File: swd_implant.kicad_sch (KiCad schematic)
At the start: 21 parts, among them J1 U262-161N-4BVC11, J2 G&W pressure contact, J3 50 mil Pin Header, J4 SOICbite, J5 100 mil Pin Header, J6 100 mil Pin header, U1 ATSAMD21E18A, U2 AP2127K-3.3

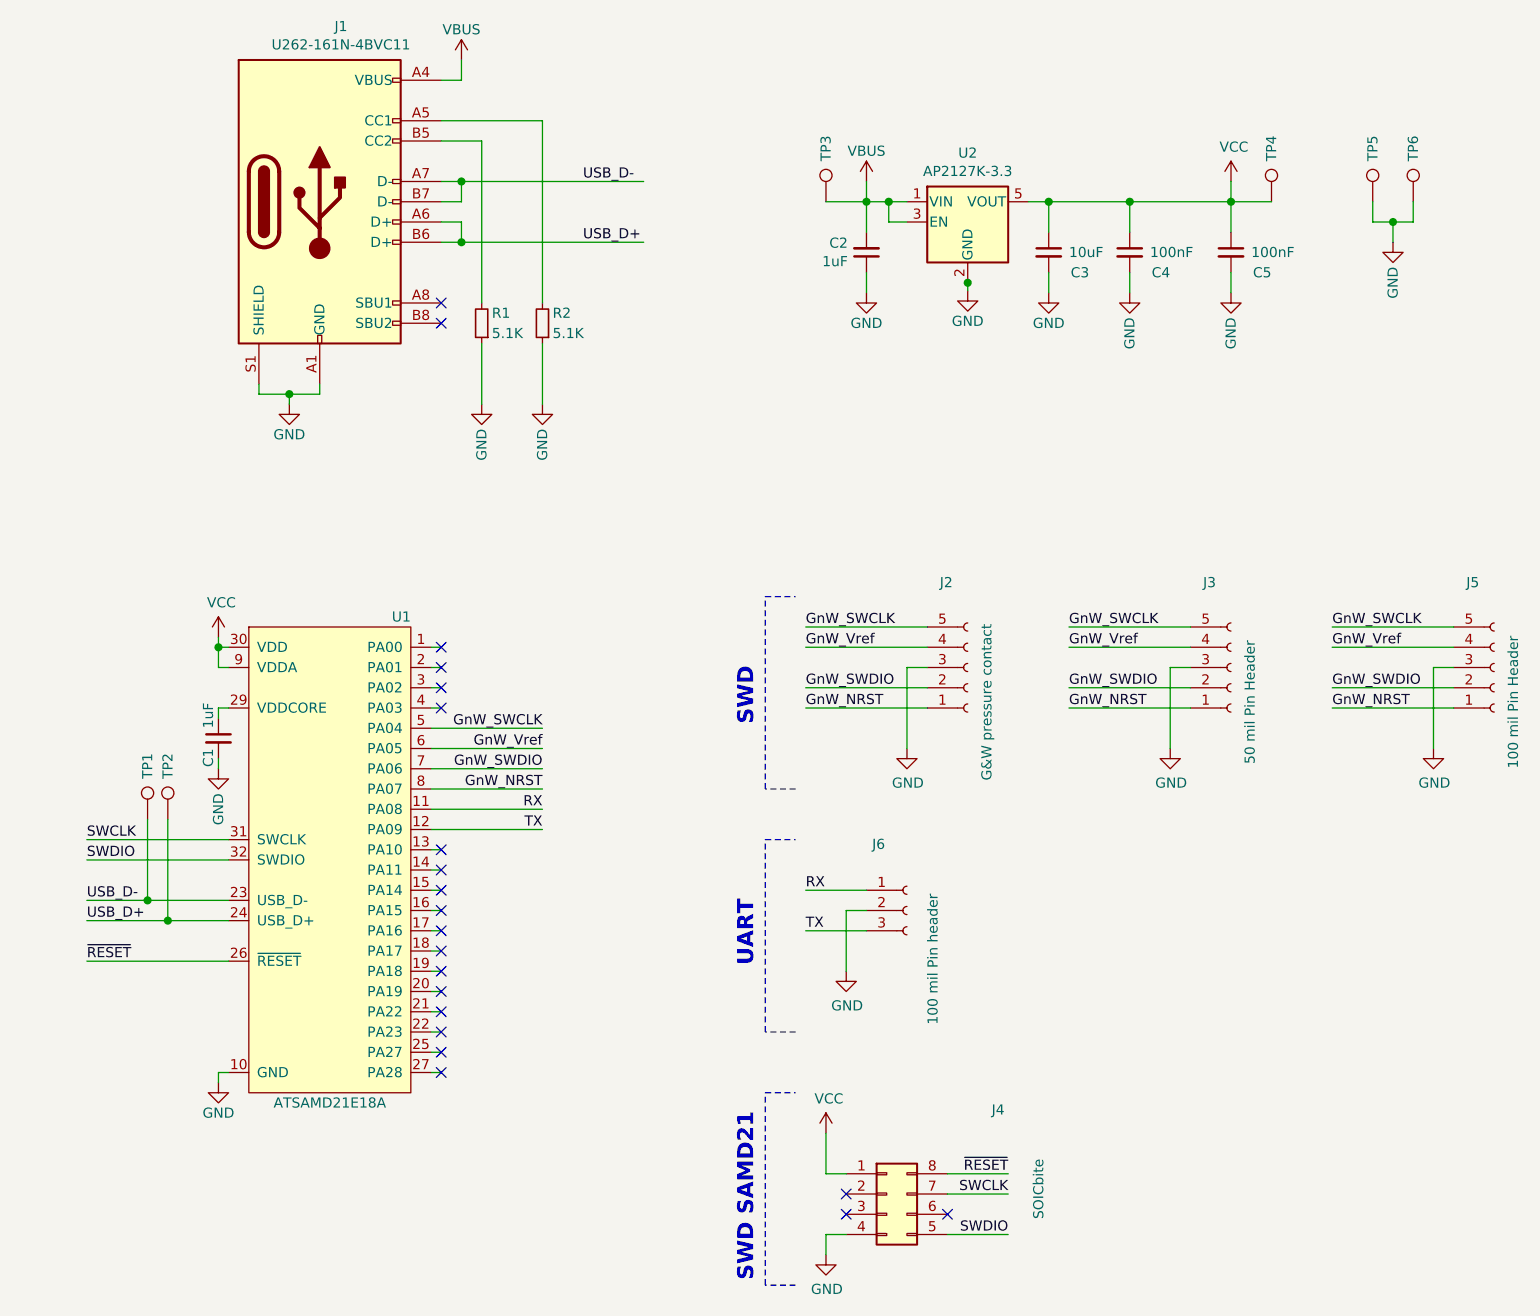
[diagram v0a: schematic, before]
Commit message: Added 10k reset pullup
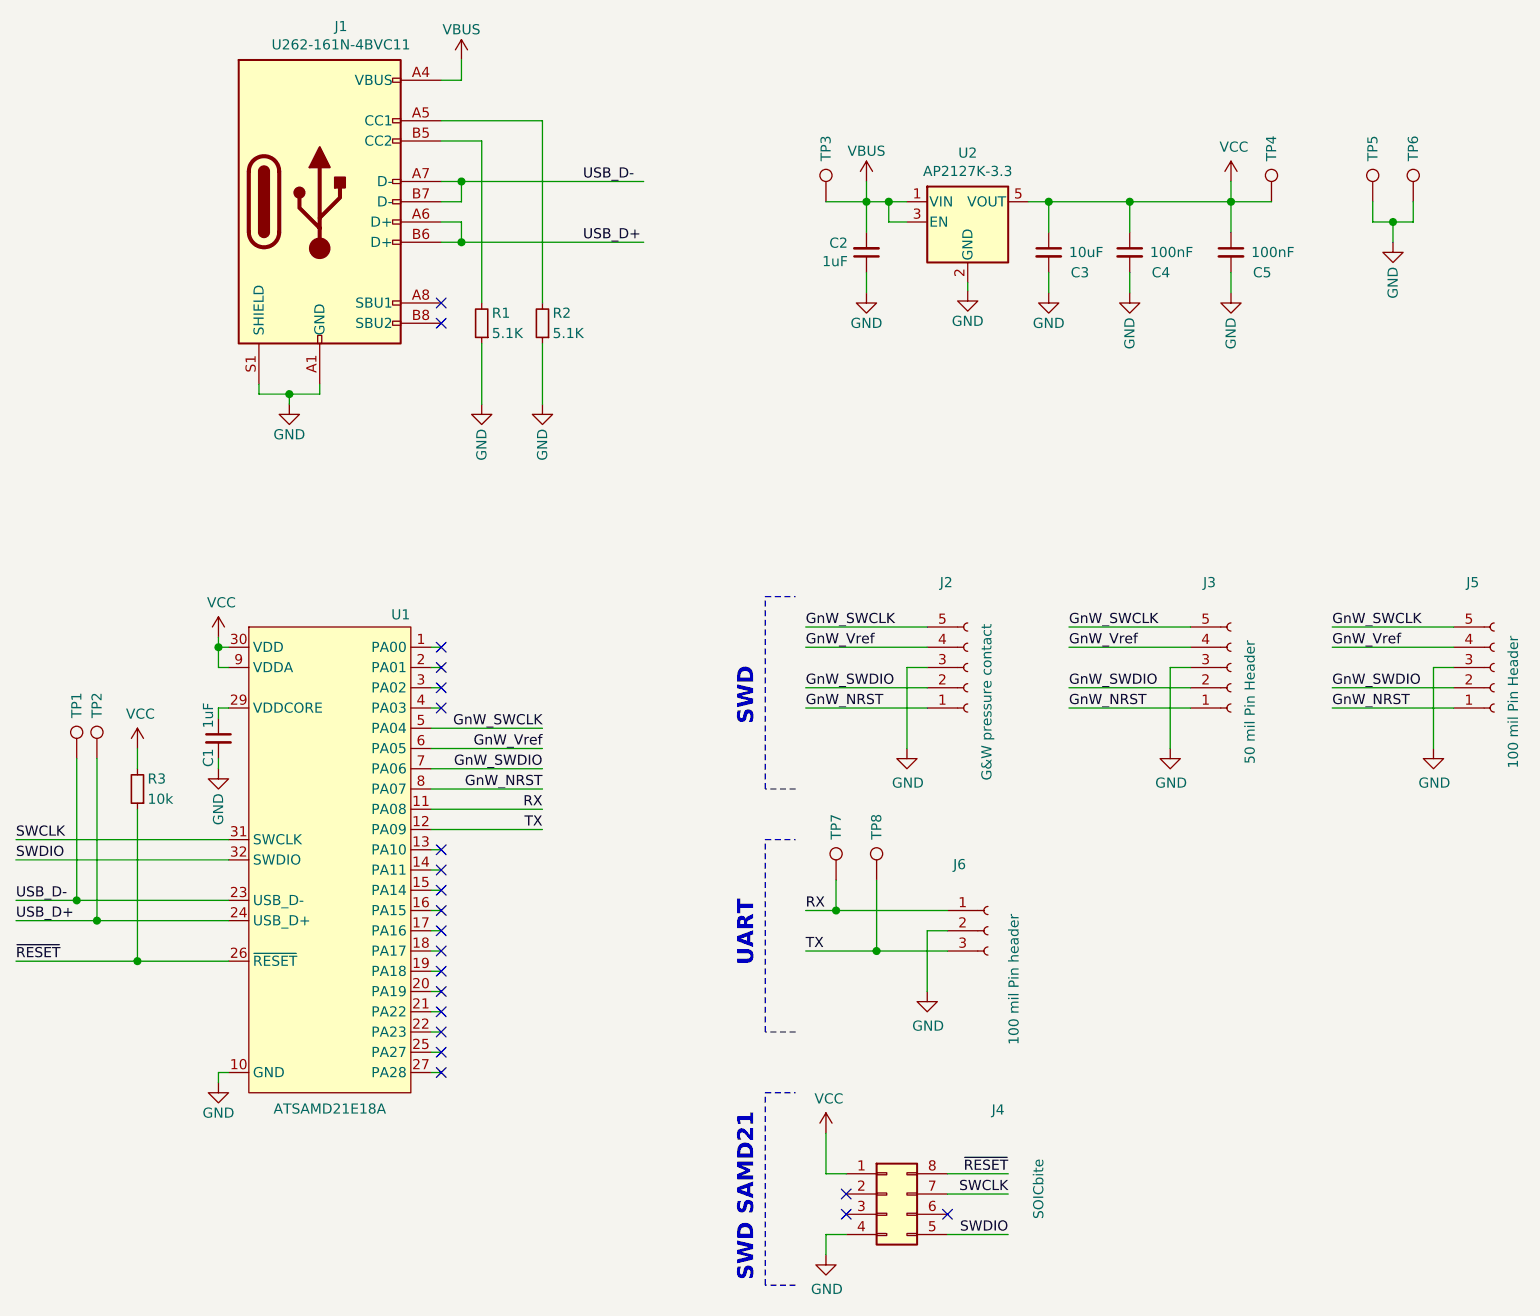
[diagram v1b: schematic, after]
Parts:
- removed U1: ATSAMD21E18A, Package_DFN_QFN:QFN-32-1EP_5x5mm_P0.5mm_EP3.6x3.6mm, symbol serpente_plug-rescue:ATSAMD21E1xA-MCU_Microchip_SAMD_Extra
- added R3: 10k, Resistor_SMD:R_0402_1005Metric, symbol Device:R_Small
- added TP7, TP8: TP_USB_D+, GnW_SWD:TestPoint_Pad_D1.0mm, symbol Connector:TestPoint
- added U1: ATSAMD21E18A, Package_DFN_QFN:QFN-32-1EP_5x5mm_P0.5mm_EP3.6x3.6mm, symbol ATSAMD21:ATSAMD21E18A
- J3: footprint Connector_PinHeader_1.27mm:PinHeader_1x05_P1.27mm_Vertical -> GnW_SWD:PinHeader_1x05_P1.27mm_Vertical
- TP1, TP2, TP3, TP4, TP5, TP6: footprint TestPoint:TestPoint_Pad_D1.0mm -> GnW_SWD:TestPoint_Pad_D1.0mm
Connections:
- net GND: now also U1.10 (GND), U1.28 (GND)
- net GnW_NRST: now also U1.8 (PA07)
- net GnW_SWCLK: now also U1.5 (PA04)
- net GnW_SWDIO: now also U1.7 (PA06)
- net GnW_Vref: now also U1.6 (PA05)
- net RX: now also TP7.1, U1.11 (PA08)
- net SWCLK: now also U1.31 (SWCLK)
- net SWDIO: now also U1.32 (SWDIO)
- net TX: now also TP8.1, U1.12 (PA09)
- net USB_D+: now also U1.24 (USB_D+)
- net USB_D-: now also U1.23 (USB_D-)
- net VCC: now also R3.2, U1.30 (VDD), U1.9 (VDDA)
- net ~RESET~: now also R3.1, U1.26 (~RESET~)
- net at C1.1: now also U1.29 (VDDCORE)
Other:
- moved on the sheet: J6, TP1, TP2
